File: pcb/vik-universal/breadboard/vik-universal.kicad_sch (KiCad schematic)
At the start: 146 parts, among them J1001 Conn_01x01_Socket

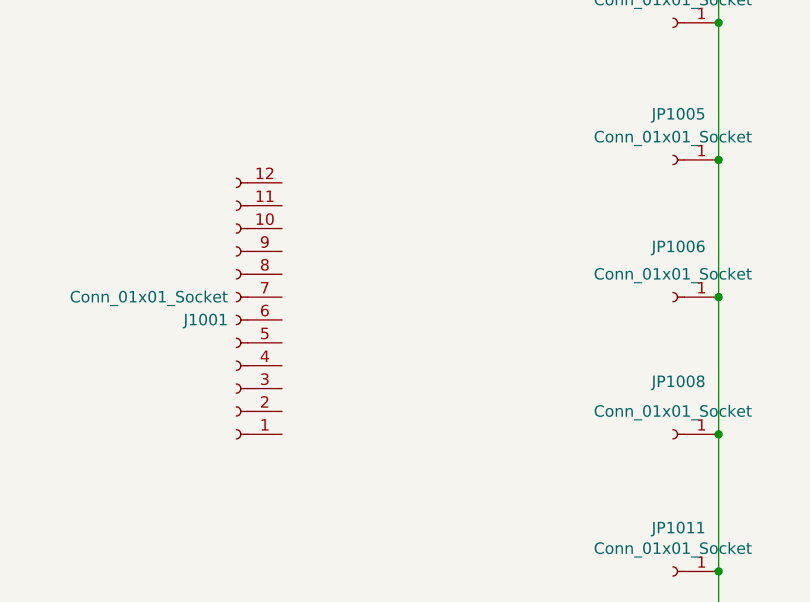
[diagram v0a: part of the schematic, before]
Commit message: Updated VIK breadboard to be 2.54mm horizontal spacing, along with a second set of numbered through holes to allow you to more easily wire up from the numbered columns to the VIK columns
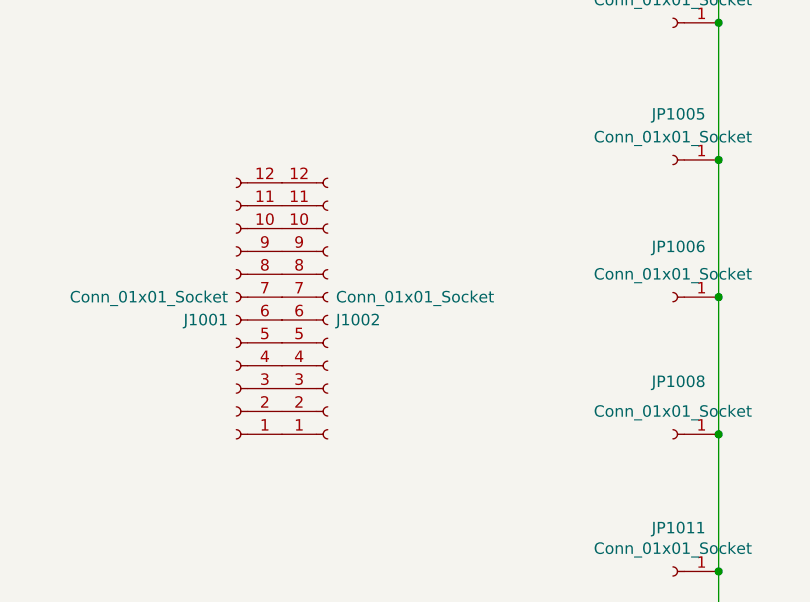
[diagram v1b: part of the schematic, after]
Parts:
- added J1002: Conn_01x01_Socket, Connector_PinSocket_2.54mm:PinSocket_1x12_P2.54mm_Vertical, symbol Connector:Conn_01x12_Socket
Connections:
- net at J1001.1 (Pin_1): now also J1002.1 (Pin_1)
- net at J1001.10 (Pin_10): now also J1002.10 (Pin_10)
- net at J1001.11 (Pin_11): now also J1002.11 (Pin_11)
- net at J1001.12 (Pin_12): now also J1002.12 (Pin_12)
- net at J1001.2 (Pin_2): now also J1002.2 (Pin_2)
- net at J1001.3 (Pin_3): now also J1002.3 (Pin_3)
- net at J1001.4 (Pin_4): now also J1002.4 (Pin_4)
- net at J1001.5 (Pin_5): now also J1002.5 (Pin_5)
- net at J1001.6 (Pin_6): now also J1002.6 (Pin_6)
- net at J1001.7 (Pin_7): now also J1002.7 (Pin_7)
- net at J1001.8 (Pin_8): now also J1002.8 (Pin_8)
- net at J1001.9 (Pin_9): now also J1002.9 (Pin_9)
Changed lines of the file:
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@@
+    )
+  )
+  (symbol (lib_id "Connector:Conn_01x12_Socket") (at 116.84 137.16 0) (mirror x) (unit 1)
+    (in_bom yes) (on_board yes) (dnp no) (fields_autoplaced)
+    (property "Reference" "J1002" (at 117.7544 137.16 0)
+      (effects (font (size 1.27 1.27)) (justify left))
+    )
+    (property "Value" "Conn_01x01_Socket" (at 117.7544 134.62 0)
+      (effects (font (size 1.27 1.27)) (justify left))
+    )
+    (property "Footprint" "Connector_PinSocket_2.54mm:PinSocket_1x12_P2.54mm_Vertical" (at 116.84 137.16 0)
+      (effects (font (size 1.27 1.27)) hide)
+    )
+    (property "Datasheet" "~" (at 116.84 137.16 0)
+      (effects (font (size 1.27 1.27)) hide)
+    )
+    (pin "1")
+    (pin "10")
+    (pin "11")
+    (pin "12")
+    (pin "2")
+    (pin "3")
+    (pin "4")
+    (pin "5")
+    (pin "6")
+    (pin "7")
+    (pin "8")
+    (pin "9")
+    (instances
+      (project "vik-universal"
+        (path "/e63e39d7-6ac0-4ffd-8aa3-1841a4541b55"
+          (reference "J1002") (unit 1)
+        )
+      )
     )
   )

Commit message: realized that the vik universal breadboard wasn't actually a breadboard at all, so I redid it to be so
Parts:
- removed JP1001, JP1002, JP1003, JP1004, JP1005, JP1006, JP1007, JP1008, JP1009, JP1010, JP1011, JP1012, JP1013, JP1014, JP1015, JP1016, JP1017, JP1018, JP1019, JP1020, JP1021, JP1022, JP1023, JP1024, JP1025, JP1026, JP1027, JP1028, JP1029, JP1030, JP1031, JP1032, JP1033, JP1034, JP1035, JP1036, JP1037, JP1038, JP1039, JP1040, JP1041, JP1042, JP1043, JP1044, JP1045, JP1046, JP1047, JP1048, JP1049, JP1050, JP1051, JP1052, JP1053, JP1054, JP1055, JP1056, JP1057, JP1058, JP1059, JP1060, JP1061, JP1062, JP1063, JP1064, JP1065, JP1066, JP1067, JP1068, JP1069, JP1070, JP1071, JP1072, JP1073, JP1074, JP1075, JP1076, JP1077, JP1078, JP1079, JP1080, JP1081, JP1082, JP1083, JP1084, JP1085, JP1086, JP1087, JP1088, JP1089, JP1090, JP1091, JP1092, JP1093, JP1094, JP1095, JP1096, JP1097, JP1098, JP1099, JP1100, JP1101, JP1102, JP1103, JP1104, JP1105, JP1106, JP1107, JP1108, JP1109, JP1110, JP1111, JP1112, JP1113, JP1114, JP1115, JP1116, JP1117, JP1118, JP1119, JP1120, JP1121, JP1122, JP1123, JP1124, JP1125, JP1126, JP1127, JP1128, JP1129, JP1130, JP1131, JP1132, JP1133, JP1134, JP1135, JP1136, JP1137, JP1138, JP1139, JP1140, JP1141, JP1142, JP1143, JP1144: Conn_01x01_Socket, fingerpunch:Pin_D1.0mm_L10.0mm_NoRef, symbol Connector:Conn_01x01_Socket
- added J1004: Conn_01x01_Socket, fingerpunch:PinSocket_1x12_P2.54mm_Vertical_IndividualSilk, symbol Connector:Conn_01x12_Socket
- added J1005, J1006, J1007, J1008, J1009, J1010, J1012, J1013, J1014, J1018, J1019, J1020: Conn_01x01_Socket, fingerpunch:PinSocket_1x12_P2.54mm_Vertical_6x6_SplitSilk, symbol Connector:Conn_01x12_Socket
- added J1011, J1015, J1016, J1017: Conn_01x01_Socket, fingerpunch:PinSocket_1x12_P2.54mm_Vertical_FullSilk, symbol Connector:Conn_01x12_Socket
- J1001, J1002: footprint Connector_PinSocket_2.54mm:PinSocket_1x12_P2.54mm_Vertical -> fingerpunch:PinSocket_1x12_P2.54mm_Vertical_NoSilk
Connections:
- net CS: now also J1004.3 (Pin_3)
- net GND: now also J1004.11 (Pin_11), J1015.1 (Pin_1), J1015.10 (Pin_10), J1015.11 (Pin_11), J1015.12 (Pin_12), J1015.2 (Pin_2), J1015.3 (Pin_3), J1015.4 (Pin_4), J1015.5 (Pin_5), J1015.6 (Pin_6), J1015.7 (Pin_7), J1015.8 (Pin_8), J1015.9 (Pin_9), J1017.1 (Pin_1), J1017.10 (Pin_10), J1017.11 (Pin_11), J1017.12 (Pin_12), J1017.2 (Pin_2), J1017.3 (Pin_3), J1017.4 (Pin_4), J1017.5 (Pin_5), J1017.6 (Pin_6), J1017.7 (Pin_7), J1017.8 (Pin_8), J1017.9 (Pin_9)
- net GPIO_AD1: now also J1004.6 (Pin_6)
- net GPIO_AD2: now also J1004.4 (Pin_4)
- net MISO: now also J1004.2 (Pin_2)
- net MOSI: now also J1004.5 (Pin_5)
- net RGB_LED_IN: now also J1004.8 (Pin_8)
- net SCL: now also J1004.9 (Pin_9)
- net SCLK: now also J1004.1 (Pin_1)
- net SDA: now also J1004.10 (Pin_10)
- net VDD_3.3V: now also J1004.12 (Pin_12), J1016.1 (Pin_1), J1016.10 (Pin_10), J1016.11 (Pin_11), J1016.12 (Pin_12), J1016.2 (Pin_2), J1016.3 (Pin_3), J1016.4 (Pin_4), J1016.5 (Pin_5), J1016.6 (Pin_6), J1016.7 (Pin_7), J1016.8 (Pin_8), J1016.9 (Pin_9)
- net VDD_5V: now also J1004.7 (Pin_7), J1011.1 (Pin_1), J1011.10 (Pin_10), J1011.11 (Pin_11), J1011.12 (Pin_12), J1011.2 (Pin_2), J1011.3 (Pin_3), J1011.4 (Pin_4), J1011.5 (Pin_5), J1011.6 (Pin_6), J1011.7 (Pin_7), J1011.8 (Pin_8), J1011.9 (Pin_9)
- new net: J1008.1 (Pin_1), J1008.2 (Pin_2), J1008.3 (Pin_3), J1008.4 (Pin_4), J1008.5 (Pin_5), J1008.6 (Pin_6)
- new net: J1008.10 (Pin_10), J1008.11 (Pin_11), J1008.12 (Pin_12), J1008.7 (Pin_7), J1008.8 (Pin_8), J1008.9 (Pin_9)
- new net: J1009.1 (Pin_1), J1009.2 (Pin_2), J1009.3 (Pin_3), J1009.4 (Pin_4), J1009.5 (Pin_5), J1009.6 (Pin_6)
- new net: J1009.10 (Pin_10), J1009.11 (Pin_11), J1009.12 (Pin_12), J1009.7 (Pin_7), J1009.8 (Pin_8), J1009.9 (Pin_9)
- new net: J1014.1 (Pin_1), J1014.2 (Pin_2), J1014.3 (Pin_3), J1014.4 (Pin_4), J1014.5 (Pin_5), J1014.6 (Pin_6)
- new net: J1014.10 (Pin_10), J1014.11 (Pin_11), J1014.12 (Pin_12), J1014.7 (Pin_7), J1014.8 (Pin_8), J1014.9 (Pin_9)
- new net: J1005.1 (Pin_1), J1005.2 (Pin_2), J1005.3 (Pin_3), J1005.4 (Pin_4), J1005.5 (Pin_5), J1005.6 (Pin_6)
- new net: J1005.10 (Pin_10), J1005.11 (Pin_11), J1005.12 (Pin_12), J1005.7 (Pin_7), J1005.8 (Pin_8), J1005.9 (Pin_9)
- new net: J1010.1 (Pin_1), J1010.2 (Pin_2), J1010.3 (Pin_3), J1010.4 (Pin_4), J1010.5 (Pin_5), J1010.6 (Pin_6)
- new net: J1010.10 (Pin_10), J1010.11 (Pin_11), J1010.12 (Pin_12), J1010.7 (Pin_7), J1010.8 (Pin_8), J1010.9 (Pin_9)
- new net: J1012.1 (Pin_1), J1012.2 (Pin_2), J1012.3 (Pin_3), J1012.4 (Pin_4), J1012.5 (Pin_5), J1012.6 (Pin_6)
- new net: J1012.10 (Pin_10), J1012.11 (Pin_11), J1012.12 (Pin_12), J1012.7 (Pin_7), J1012.8 (Pin_8), J1012.9 (Pin_9)
- new net: J1019.1 (Pin_1), J1019.2 (Pin_2), J1019.3 (Pin_3), J1019.4 (Pin_4), J1019.5 (Pin_5), J1019.6 (Pin_6)
- new net: J1019.10 (Pin_10), J1019.11 (Pin_11), J1019.12 (Pin_12), J1019.7 (Pin_7), J1019.8 (Pin_8), J1019.9 (Pin_9)
- new net: J1006.1 (Pin_1), J1006.2 (Pin_2), J1006.3 (Pin_3), J1006.4 (Pin_4), J1006.5 (Pin_5), J1006.6 (Pin_6)
- new net: J1006.10 (Pin_10), J1006.11 (Pin_11), J1006.12 (Pin_12), J1006.7 (Pin_7), J1006.8 (Pin_8), J1006.9 (Pin_9)
- new net: J1020.1 (Pin_1), J1020.2 (Pin_2), J1020.3 (Pin_3), J1020.4 (Pin_4), J1020.5 (Pin_5), J1020.6 (Pin_6)
- new net: J1020.10 (Pin_10), J1020.11 (Pin_11), J1020.12 (Pin_12), J1020.7 (Pin_7), J1020.8 (Pin_8), J1020.9 (Pin_9)
- new net: J1007.1 (Pin_1), J1007.2 (Pin_2), J1007.3 (Pin_3), J1007.4 (Pin_4), J1007.5 (Pin_5), J1007.6 (Pin_6)
- new net: J1007.10 (Pin_10), J1007.11 (Pin_11), J1007.12 (Pin_12), J1007.7 (Pin_7), J1007.8 (Pin_8), J1007.9 (Pin_9)
- new net: J1018.1 (Pin_1), J1018.2 (Pin_2), J1018.3 (Pin_3), J1018.4 (Pin_4), J1018.5 (Pin_5), J1018.6 (Pin_6)
- new net: J1018.10 (Pin_10), J1018.11 (Pin_11), J1018.12 (Pin_12), J1018.7 (Pin_7), J1018.8 (Pin_8), J1018.9 (Pin_9)
- new net: J1013.1 (Pin_1), J1013.2 (Pin_2), J1013.3 (Pin_3), J1013.4 (Pin_4), J1013.5 (Pin_5), J1013.6 (Pin_6)
- new net: J1013.10 (Pin_10), J1013.11 (Pin_11), J1013.12 (Pin_12), J1013.7 (Pin_7), J1013.8 (Pin_8), J1013.9 (Pin_9)
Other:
- moved on the sheet: J1001, J1002, J1003

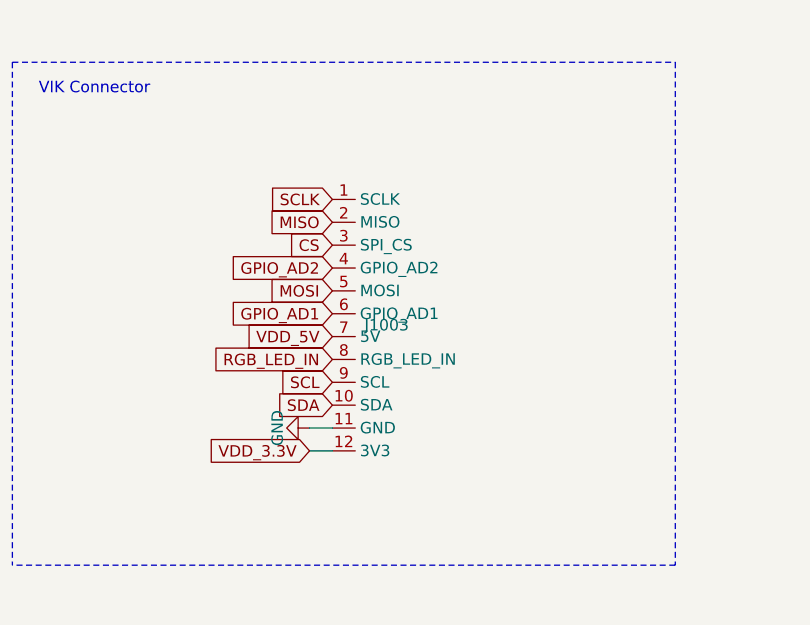
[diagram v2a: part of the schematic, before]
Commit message: updated vikm connector symbols, per some recommendations from sigprof in fingerpunch discord
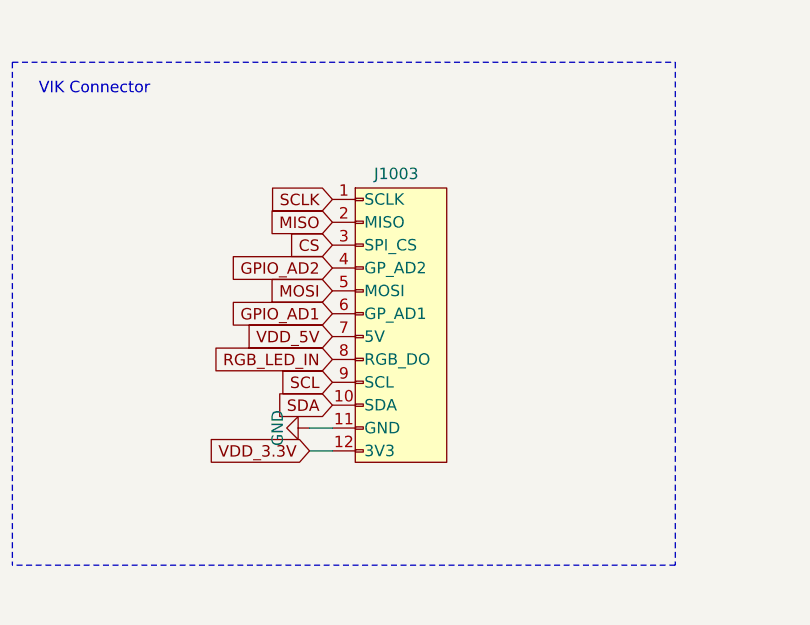
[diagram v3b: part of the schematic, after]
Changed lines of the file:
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@@
     )
   )
-  (symbol (lib_id "vik:vik-module-connector") (at 296.418 64.008 0) (unit 1)
-    (in_bom yes) (on_board yes) (dnp no) (fields_autoplaced)
-    (property "Reference" "J1003" (at 299.974 64.008 0)
+  (symbol (lib_id "vik:vik-module-connector") (at 304.038 62.738 0) (unit 1)
+    (in_bom yes) (on_board yes) (dnp no)
+    (property "Reference" "J1003" (at 301.0408 47.1932 0)
       (effects (font (size 1.27 1.27)) (justify left))
     )
-    (property "Value" "~" (at 296.418 57.658 0)
+    (property "Value" "~" (at 304.038 56.388 0)
       (effects (font (size 1.27 1.27)))
     )
-    (property "Footprint" "vik:vik-module-connector-horizontal" (at 296.418 57.658 0)
+    (property "Footprint" "vik:vik-module-connector-horizontal" (at 304.038 56.388 0)
       (effects (font (size 1.27 1.27)) hide)
     )
-    (property "Datasheet" "" (at 296.418 57.658 0)
+    (property "Datasheet" "" (at 304.038 56.388 0)
       (effects (font (size 1.27 1.27)) hide)
     )
-    (property "LCSC" "C2919557" (at 296.418 64.008 0)
+    (property "LCSC" "C2919557" (at 304.038 62.738 0)
       (effects (font (size 1.27 1.27)) hide)
     )
